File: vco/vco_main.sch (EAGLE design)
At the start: 101 parts, among them IC1 OPA4130U, IC2 LM13700M, IC3 OPA4130U, IC4 OPA4130U, Q1 MMBFJ3

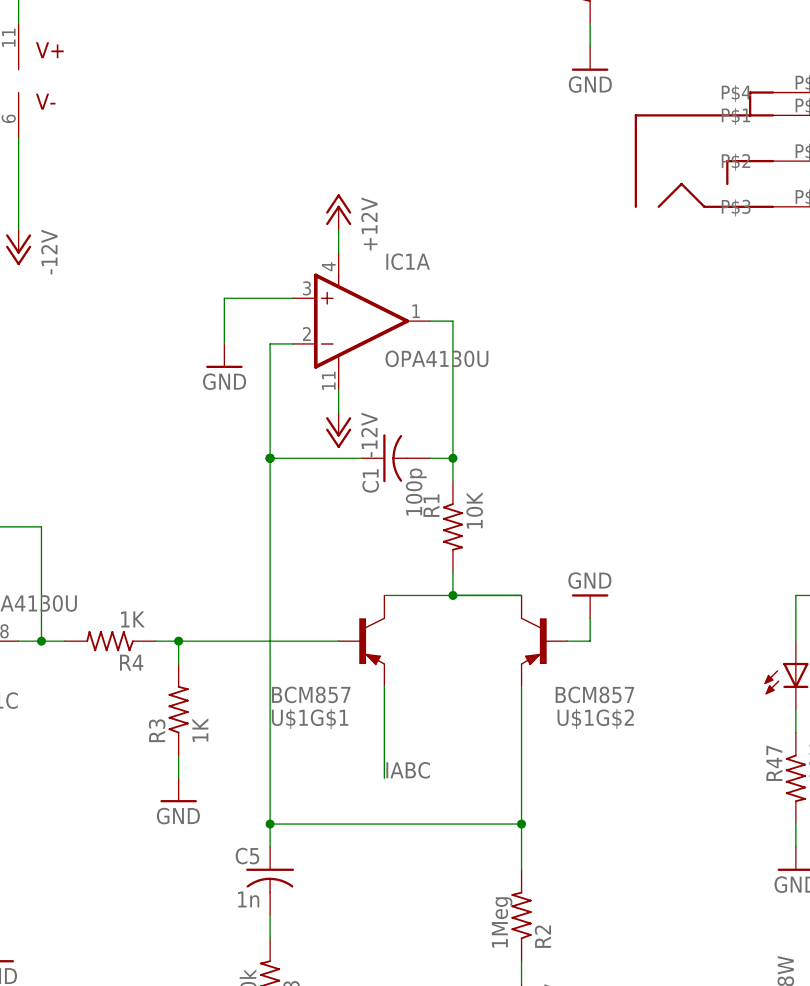
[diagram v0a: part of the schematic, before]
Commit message: flipped the pnp pair right side up in schematic.
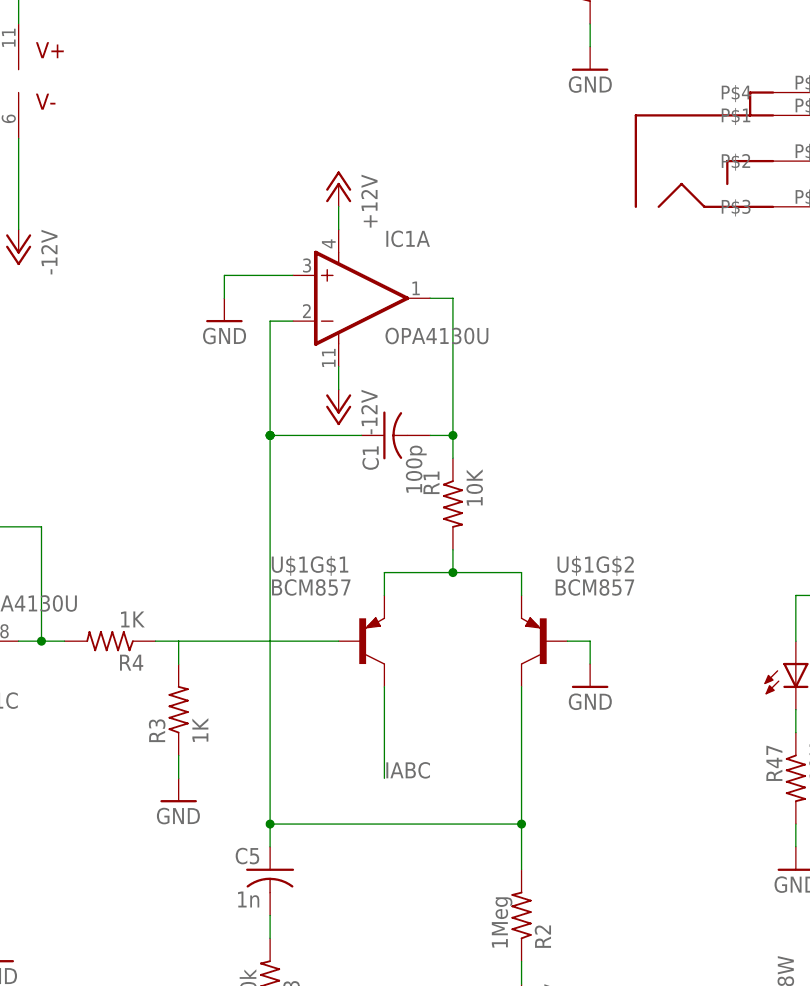
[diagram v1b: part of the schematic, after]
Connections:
- removed net N$1: R1.2, U$1G$1.C, U$1G$2.C
- new net N$12: R1.2, U$1G$1.E, U$1G$2.E
- net IABC: now also U$1G$1.C; no longer U$1G$1.E
- net N$3: now also U$1G$2.C; no longer U$1G$2.E
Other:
- moved on the sheet: C1, IC1A, R1, U$1G$1, U$1G$2
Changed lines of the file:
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@@
 </plain>
 <instances>
-<instance part="U$1" gate="G$1" x="71.12" y="15.24" rot="MR180"/>
-<instance part="U$1" gate="G$2" x="91.44" y="15.24" rot="R180"/>
-<instance part="IC1" gate="A" x="71.12" y="50.8"/>
+<instance part="U$1" gate="G$1" x="71.12" y="15.24"/>
+<instance part="U$1" gate="G$2" x="91.44" y="15.24" rot="MR0"/>
+<instance part="IC1" gate="A" x="71.12" y="53.34"/>
 <instance part="IC1" gate="B" x="81.28" y="124.46" rot="MR180"/>
 <instance part="IC1" gate="C" x="25.4" y="15.24" rot="MR180"/>
 <instance part="IC1" gate="D" x="172.72" y="43.18"/>
-<instance part="R1" gate="G$1" x="81.28" y="27.94" rot="MR270"/>
+<instance part="R1" gate="G$1" x="81.28" y="30.48" rot="MR270"/>
 <instance part="R2" gate="G$1" x="88.9" y="-15.24" rot="MR90"/>
-<instance part="GND1" gate="1" x="55.88" y="45.72" rot="MR0"/>
-<instance part="P+1" gate="1" x="68.58" y="63.5" rot="MR0"/>
-<instance part="P-1" gate="1" x="68.58" y="38.1" rot="MR0"/>
-<instance part="GND2" gate="1" x="96.52" y="20.32" rot="MR180"/>
+<instance part="GND1" gate="1" x="55.88" y="50.8" rot="MR0"/>
+<instance part="P+1" gate="1" x="68.58" y="66.04" rot="MR0"/>
+<instance part="P-1" gate="1" x="68.58" y="40.64" rot="MR0"/>
+<instance part="GND2" gate="1" x="96.52" y="10.16" rot="MR0"/>
 <instance part="R3" gate="G$1" x="50.8" y="7.62" rot="R90"/>
 <instance part="R4" gate="G$1" x="43.18" y="15.24" rot="R180"/>
@@
 <instance part="IC2" gate="G$3" x="-91.44" y="71.12"/>
 <instance part="IC2" gate="G$4" x="-91.44" y="63.5"/>
-<instance part="C1" gate="G$1" x="73.66" y="35.56" rot="MR270"/>
+<instance part="C1" gate="G$1" x="73.66" y="38.1" rot="MR270"/>
 <instance part="FINE" gate="G$1" x="-48.26" y="27.94"/>
 <instance part="R14" gate="G$1" x="-48.26" y="43.18" rot="R90"/>
@@
 </busses>
 <nets>
-<net name="N$1" class="0">
-<segment>
-<pinref part="U$1" gate="G$1" pin="C"/>
-<pinref part="U$1" gate="G$2" pin="C"/>
-<wire x1="73.66" y1="20.32" x2="81.28" y2="20.32" width="0.1524" layer="91"/>
-<wire x1="81.28" y1="20.32" x2="88.9" y2="20.32" width="0.1524" layer="91"/>
-<wire x1="88.9" y1="20.32" x2="81.28" y2="20.32" width="0.1524" layer="91"/>
-<wire x1="81.28" y1="20.32" x2="81.28" y2="22.86" width="0.1524" layer="91"/>
-<pinref part="R1" gate="G$1" pin="2"/>
-<junction x="81.28" y="20.32"/>
-</segment>
-</net>
 <net name="N$2" class="0">
 <segment>
 <pinref part="IC1" gate="A" pin="OUT"/>
 <pinref part="R1" gate="G$1" pin="1"/>
-<wire x1="78.74" y1="50.8" x2="81.28" y2="50.8" width="0.1524" layer="91"/>
-<wire x1="81.28" y1="50.8" x2="81.28" y2="35.56" width="0.1524" layer="91"/>
+<wire x1="78.74" y1="53.34" x2="81.28" y2="53.34" width="0.1524" layer="91"/>
+<wire x1="81.28" y1="53.34" x2="81.28" y2="38.1" width="0.1524" layer="91"/>
 <pinref part="C1" gate="G$1" pin="2"/>
-<wire x1="81.28" y1="35.56" x2="81.28" y2="33.02" width="0.1524" layer="91"/>
-<wire x1="78.74" y1="35.56" x2="81.28" y2="35.56" width="0.1524" layer="91"/>
-<junction x="81.28" y="35.56"/>
+<wire x1="81.28" y1="38.1" x2="81.28" y2="35.56" width="0.1524" layer="91"/>
+<wire x1="78.74" y1="38.1" x2="81.28" y2="38.1" width="0.1524" layer="91"/>
+<junction x="81.28" y="38.1"/>
 </segment>
 </net>
@@
 <segment>
 <pinref part="IC1" gate="A" pin="-IN"/>
-<wire x1="63.5" y1="48.26" x2="60.96" y2="48.26" width="0.1524" layer="91"/>
-<wire x1="60.96" y1="48.26" x2="60.96" y2="35.56" width="0.1524" layer="91"/>
+<wire x1="63.5" y1="50.8" x2="60.96" y2="50.8" width="0.1524" layer="91"/>
+<wire x1="60.96" y1="50.8" x2="60.96" y2="38.1" width="0.1524" layer="91"/>
 <pinref part="C1" gate="G$1" pin="1"/>
-<wire x1="71.12" y1="35.56" x2="60.96" y2="35.56" width="0.1524" layer="91"/>
+<wire x1="71.12" y1="38.1" x2="60.96" y2="38.1" width="0.1524" layer="91"/>
 <pinref part="C5" gate="G$1" pin="1"/>
 <wire x1="60.96" y1="-7.62" x2="60.96" y2="-5.08" width="0.1524" layer="91"/>
 <pinref part="R2" gate="G$1" pin="2"/>
-<pinref part="U$1" gate="G$2" pin="E"/>
-<wire x1="88.9" y1="-5.08" x2="88.9" y2="10.16" width="0.1524" layer="91"/>
 <wire x1="60.96" y1="-5.08" x2="88.9" y2="-5.08" width="0.1524" layer="91"/>
 <wire x1="88.9" y1="-5.08" x2="88.9" y2="-10.16" width="0.1524" layer="91"/>
+<wire x1="60.96" y1="38.1" x2="60.96" y2="-5.08" width="0.1524" layer="91"/>
+<junction x="60.96" y="-5.08"/>
+<junction x="60.96" y="38.1"/>
+<junction x="60.96" y="38.1"/>
+<pinref part="U$1" gate="G$2" pin="C"/>
+<wire x1="88.9" y1="10.16" x2="88.9" y2="-5.08" width="0.1524" layer="91"/>
 <junction x="88.9" y="-5.08"/>
-<wire x1="60.96" y1="35.56" x2="60.96" y2="-5.08" width="0.1524" layer="91"/>
-<junction x="60.96" y="-5.08"/>
-<junction x="60.96" y="35.56"/>
-<junction x="60.96" y="35.56"/>
 </segment>
 </net>
@@
 <segment>
 <pinref part="IC1" gate="A" pin="V-"/>
-<wire x1="68.58" y1="43.18" x2="68.58" y2="40.64" width="0.1524" layer="91"/>
+<wire x1="68.58" y1="45.72" x2="68.58" y2="43.18" width="0.1524" layer="91"/>
 <pinref part="P-1" gate="1" pin="-12V"/>
 </segment>
@@
 <segment>
 <pinref part="IC1" gate="A" pin="V+"/>
-<wire x1="68.58" y1="58.42" x2="68.58" y2="60.96" width="0.1524" layer="91"/>
+<wire x1="68.58" y1="60.96" x2="68.58" y2="63.5" width="0.1524" layer="91"/>
 <pinref part="P+1" gate="1" pin="+12V"/>
 </segment>
@@
 <segment>
 <pinref part="GND1" gate="1" pin="GND"/>
-<wire x1="55.88" y1="48.26" x2="55.88" y2="53.34" width="0.1524" layer="91"/>
+<wire x1="55.88" y1="53.34" x2="55.88" y2="55.88" width="0.1524" layer="91"/>
 <pinref part="IC1" gate="A" pin="+IN"/>
-<wire x1="55.88" y1="53.34" x2="63.5" y2="53.34" width="0.1524" layer="91"/>
-</segment>
-<segment>
-<pinref part="U$1" gate="G$2" pin="B"/>
-<wire x1="93.98" y1="15.24" x2="96.52" y2="15.24" width="0.1524" layer="91"/>
-<pinref part="GND2" gate="1" pin="GND"/>
-<wire x1="96.52" y1="15.24" x2="96.52" y2="17.78" width="0.1524" layer="91"/>
+<wire x1="55.88" y1="55.88" x2="63.5" y2="55.88" width="0.1524" layer="91"/>
 </segment>
 <segment>
@@
 <wire x1="43.18" y1="-50.8" x2="43.18" y2="-48.26" width="0.1524" layer="91"/>
 </segment>
+<segment>
+<pinref part="U$1" gate="G$2" pin="B"/>
+<wire x1="93.98" y1="15.24" x2="96.52" y2="15.24" width="0.1524" layer="91"/>
+<pinref part="GND2" gate="1" pin="GND"/>
+<wire x1="96.52" y1="15.24" x2="96.52" y2="12.7" width="0.1524" layer="91"/>
+</segment>
 </net>
 <net name="N$7" class="0">
@@
 <pinref part="U$1" gate="G$1" pin="B"/>
 <wire x1="68.58" y1="15.24" x2="50.8" y2="15.24" width="0.1524" layer="91"/>
-<junction x="50.8" y="15.24"/>
 </segment>
 </net>
@@
 <net name="IABC" class="0">
 <segment>
-<pinref part="U$1" gate="G$1" pin="E"/>
-<wire x1="73.66" y1="10.16" x2="73.66" y2="0" width="0.1524" layer="91"/>
-<label x="73.66" y="0" size="1.778" layer="95"/>
-</segment>
-<segment>
 <pinref part="IC2" gate="A" pin="IABC"/>
 <wire x1="58.42" y1="121.92" x2="58.42" y2="114.3" width="0.1524" layer="91"/>
 <label x="58.42" y="114.3" size="1.778" layer="95"/>
+</segment>
+<segment>
+<pinref part="U$1" gate="G$1" pin="C"/>
+<wire x1="73.66" y1="10.16" x2="73.66" y2="0" width="0.1524" layer="91"/>
+<label x="73.66" y="0" size="1.778" layer="95"/>
 </segment>
 </net>
@@
 </segment>
 </net>
+<net name="N$12" class="0">
+<segment>
+<pinref part="U$1" gate="G$2" pin="E"/>
+<wire x1="88.9" y1="20.32" x2="88.9" y2="22.86" width="0.1524" layer="91"/>
+<pinref part="U$1" gate="G$1" pin="E"/>
+<wire x1="88.9" y1="22.86" x2="81.28" y2="22.86" width="0.1524" layer="91"/>
+<wire x1="81.28" y1="22.86" x2="73.66" y2="22.86" width="0.1524" layer="91"/>
+<wire x1="73.66" y1="22.86" x2="73.66" y2="20.32" width="0.1524" layer="91"/>
+<pinref part="R1" gate="G$1" pin="2"/>
+<wire x1="81.28" y1="25.4" x2="81.28" y2="22.86" width="0.1524" layer="91"/>
+<junction x="81.28" y="22.86"/>
+</segment>
+</net>

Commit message: made changes to the vcf board
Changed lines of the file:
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@@
 <wire x1="127" y1="139.7" x2="127" y2="144.78" width="0.1524" layer="91"/>
 <pinref part="P+3" gate="1" pin="+12V"/>
+<junction x="127" y="139.7"/>
 </segment>
 <segment>
@@
 <pinref part="GND7" gate="1" pin="GND"/>
 <wire x1="71.12" y1="121.92" x2="71.12" y2="119.38" width="0.1524" layer="91"/>
-<wire x1="71.12" y1="119.38" x2="71.12" y2="116.84" width="0.1524" layer="91"/>
 </segment>
 <segment>
@@
 <wire x1="-2.54" y1="-58.42" x2="-2.54" y2="-55.88" width="0.1524" layer="91"/>
 <junction x="0" y="-55.88"/>
+<junction x="-2.54" y="-55.88"/>
 </segment>
 <segment>
@@
 <pinref part="U$1" gate="G$1" pin="B"/>
 <wire x1="68.58" y1="15.24" x2="50.8" y2="15.24" width="0.1524" layer="91"/>
+<junction x="50.8" y="15.24"/>
 </segment>
 </net>
@@
 <pinref part="LED1" gate="G$1" pin="A"/>
 <wire x1="119.38" y1="20.32" x2="119.38" y2="15.24" width="0.1524" layer="91"/>
-</segment>
-</net>
+<junction x="127" y="20.32"/>
+</segment>
+</net>

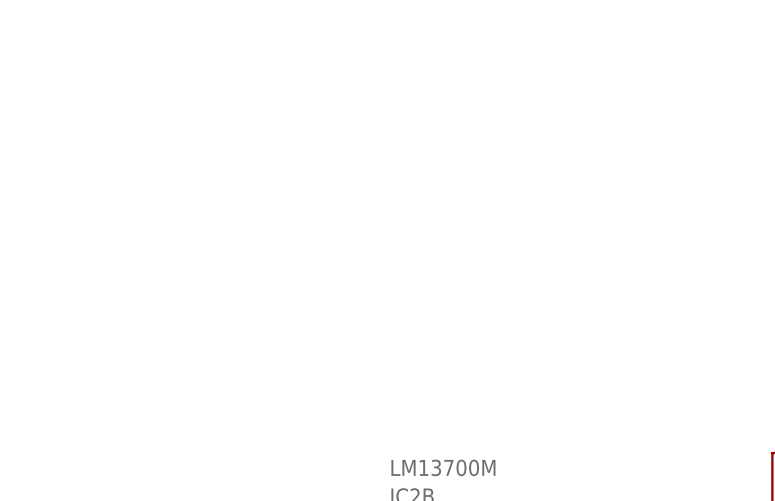
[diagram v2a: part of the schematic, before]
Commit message: got the boards!  adding notes on component changes to schematic.
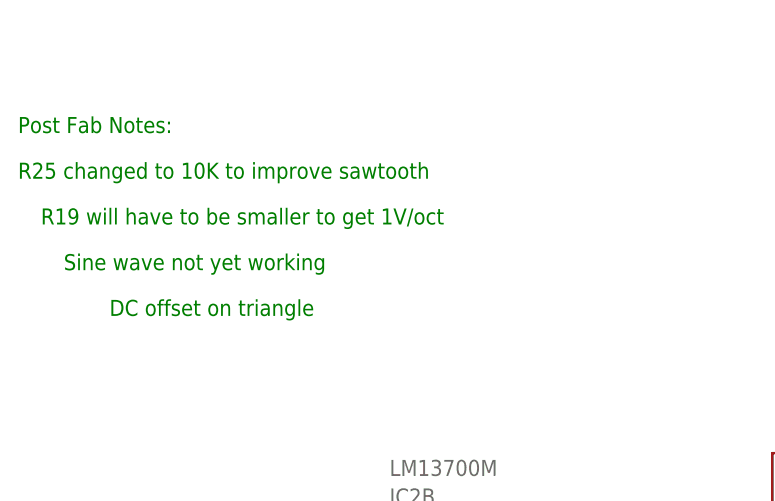
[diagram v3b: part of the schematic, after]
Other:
- note added: "DC offset on triangle"
- note added: "Post Fab Notes:"
- note added: "R19 will have to be smaller to get 1V/oct"
- note added: "R25 changed to 10K to improve sawtooth"
- note added: "Sine wave not yet working"
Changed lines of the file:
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@@
 <plain>
 <text x="165.1" y="132.08" size="1.778" layer="91">Verify location of sync input</text>
+<text x="-124.46" y="154.94" size="1.778" layer="91">Post Fab Notes:</text>
+<text x="-124.46" y="149.86" size="1.778" layer="91">R25 changed to 10K to improve sawtooth</text>
+<text x="-121.92" y="144.78" size="1.778" layer="91">R19 will have to be smaller to get 1V/oct</text>
+<text x="-119.38" y="139.7" size="1.778" layer="91">Sine wave not yet working</text>
+<text x="-114.3" y="134.62" size="1.778" layer="91">DC offset on triangle</text>
 </plain>
 <instances>

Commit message: added some more notes
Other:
- note added: "C3 is DNP"
- note added: "C4 is 1u"
- note added: "DC offset on triangle (look at R7 and R6)"
- note added: "R19 will is 5K"
- note removed: "DC offset on triangle"
- note removed: "R19 will have to be smaller to get 1V/oct"
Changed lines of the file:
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@@
 <text x="-124.46" y="154.94" size="1.778" layer="91">Post Fab Notes:</text>
 <text x="-124.46" y="149.86" size="1.778" layer="91">R25 changed to 10K to improve sawtooth</text>
-<text x="-121.92" y="144.78" size="1.778" layer="91">R19 will have to be smaller to get 1V/oct</text>
+<text x="-121.92" y="144.78" size="1.778" layer="91">R19 will is 5K </text>
 <text x="-119.38" y="139.7" size="1.778" layer="91">Sine wave not yet working</text>
-<text x="-114.3" y="134.62" size="1.778" layer="91">DC offset on triangle</text>
+<text x="-114.3" y="134.62" size="1.778" layer="91">DC offset on triangle (look at R7 and R6)</text>
+<text x="-111.76" y="129.54" size="1.778" layer="91">C3 is DNP</text>
+<text x="-109.22" y="124.46" size="1.778" layer="91">C4 is 1u</text>
 </plain>
 <instances>

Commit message: improved notes
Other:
- note added: "Add polarities for diodes, LED, pairs."
- note added: "C5 is 1u"
- note added: "R19 will is 5K, needed to provide 1V/Oct"
- note removed: "R19 will is 5K"
- note removed: "Sine wave not yet working"
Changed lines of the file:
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@@
 <plain>
 <text x="165.1" y="132.08" size="1.778" layer="91">Verify location of sync input</text>
-<text x="-124.46" y="154.94" size="1.778" layer="91">Post Fab Notes:</text>
-<text x="-124.46" y="149.86" size="1.778" layer="91">R25 changed to 10K to improve sawtooth</text>
-<text x="-121.92" y="144.78" size="1.778" layer="91">R19 will is 5K </text>
-<text x="-119.38" y="139.7" size="1.778" layer="91">Sine wave not yet working</text>
-<text x="-114.3" y="134.62" size="1.778" layer="91">DC offset on triangle (look at R7 and R6)</text>
-<text x="-111.76" y="129.54" size="1.778" layer="91">C3 is DNP</text>
-<text x="-109.22" y="124.46" size="1.778" layer="91">C4 is 1u</text>
+<text x="-121.92" y="154.94" size="1.778" layer="91">Post Fab Notes:</text>
+<text x="-121.92" y="149.86" size="1.778" layer="91">R25 changed to 10K to improve sawtooth</text>
+<text x="-121.92" y="144.78" size="1.778" layer="91">R19 will is 5K, needed to provide 1V/Oct</text>
+<text x="-121.92" y="124.46" size="1.778" layer="91">DC offset on triangle (look at R7 and R6)</text>
+<text x="-121.92" y="139.7" size="1.778" layer="91">C3 is DNP</text>
+<text x="-121.92" y="134.62" size="1.778" layer="91">C4 is 1u</text>
+<text x="-121.92" y="129.54" size="1.778" layer="91">C5 is 1u</text>
+<text x="-121.92" y="119.38" size="1.778" layer="91">Add polarities for diodes, LED, pairs.</text>
 </plain>
 <instances>
